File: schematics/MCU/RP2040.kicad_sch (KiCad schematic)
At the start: 38 parts, among them J2 Conn_ARM_SWD_TagConnect_TC203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, Q1 2N7002VC-7, SW1 TL3780AF240QG, U3 XC6210B332MR, U4 GD25Q127CWIGR

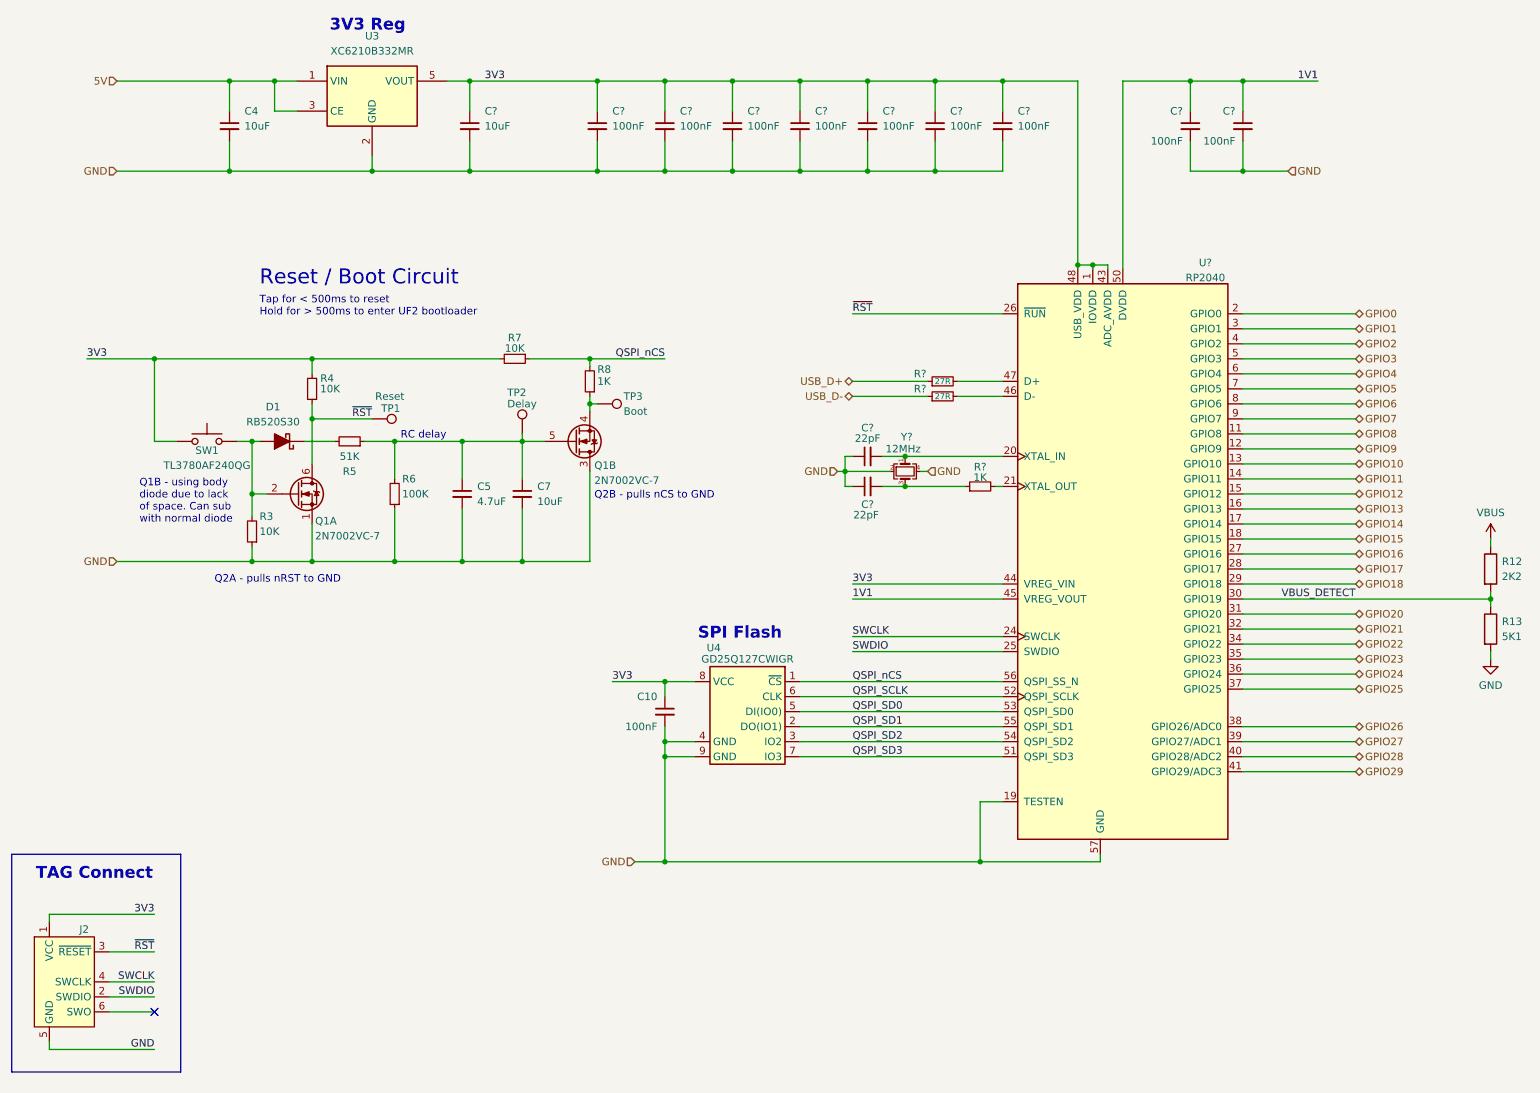
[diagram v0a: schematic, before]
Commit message: Minor refactor, add RP2040 controller schematic
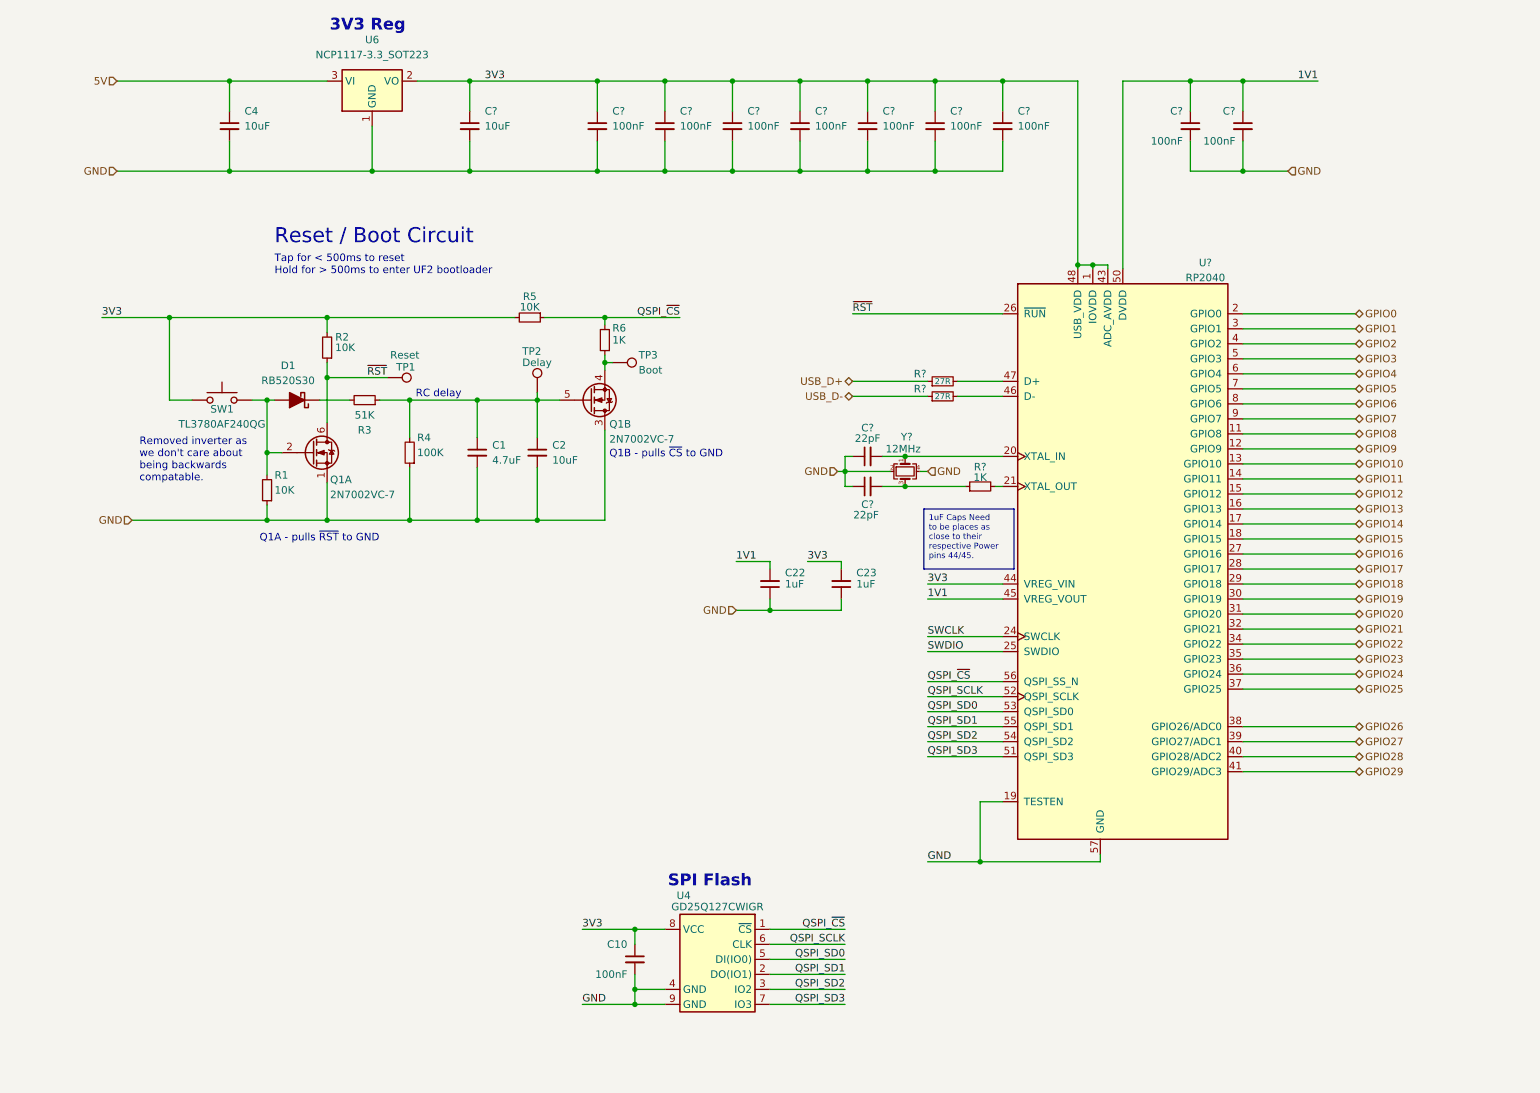
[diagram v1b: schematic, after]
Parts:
- removed C5: 4.7uF, Capacitor_SMD:C_0805_2012Metric, symbol Device:C_Small
- removed C7: 10uF, Capacitor_SMD:C_0805_2012Metric, symbol Device:C_Small
- removed J2: Conn_ARM_SWD_TagConnect_TC2030-NL, Connector:Tag-Connect_TC2030-IDC-NL_2x03_P1.27mm_Vertical, symbol Connector:Conn_ARM_SWD_TagConnect_TC2030-NL
- removed R12: 2K2, Resistor_SMD:R_0402_1005Metric, symbol Device:R
- removed R13: 5K1, Resistor_SMD:R_0402_1005Metric, symbol Device:R
- removed R7: 10K, Resistor_SMD:R_0402_1005Metric, symbol Device:R_Small
- removed R8: 1K, Resistor_SMD:R_0402_1005Metric, symbol Device:R_Small
- removed U3: XC6210B332MR, Package_TO_SOT_SMD:SOT-23-5, symbol Regulator_Linear:XC6210B332MR
- added C1: 4.7uF, Capacitor_SMD:C_0805_2012Metric, symbol Device:C_Small
- added C2: 10uF, Capacitor_SMD:C_0805_2012Metric, symbol Device:C_Small
- added C22, C23: 1uF, Capacitor_SMD:C_0603_1608Metric, symbol Device:C_Small
- added R1, R2: 10K, Resistor_SMD:R_0402_1005Metric, symbol Device:R_Small
- added U6: NCP1117-3.3_SOT223, Package_TO_SOT_SMD:SOT-223-3_TabPin2, symbol Regulator_Linear:NCP1117-3.3_SOT223
- C4, C?: footprint Capacitor_SMD:C_0402_1005Metric -> Capacitor_SMD:C_0805_2012Metric
- R3: value 10K -> 51K; MPN RC0402FR-0710KL -> RC0402FR-0751KL; Rating RES 10K OHM 1% 1/16W 0402 -> RES 51K OHM 1% 1/16W 0402; Supplier PN 311-10.0KLRCT-ND -> 311-51.0KLRCT-ND
- R4: value 10K -> 100K; MPN RC0402FR-0710KL -> RC0402FR-07100KL; Rating RES 10K OHM 1% 1/16W 0402 -> RES 100K OHM 1% 1/16W 0402; Supplier PN 311-10.0KLRCT-ND -> 311-100KLRCT-ND
- R5: value 51K -> 10K; MPN RC0402FR-0751KL -> RC0402FR-0710KL; Rating RES 51K OHM 1% 1/16W 0402 -> RES 10K OHM 1% 1/16W 0402; Supplier PN 311-51.0KLRCT-ND -> 311-10.0KLRCT-ND
- R6: value 100K -> 1K; MPN RC0402FR-07100KL -> RC0402FR-071KL; Rating RES 100K OHM 1% 1/16W 0402 -> RES 1K OHM 1% 1/16W 0402; Supplier PN 311-100KLRCT-ND -> 311-1.00KLRCT-ND
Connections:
- net 1V1: now also C22.2
- net 3V3: now also R5.2, C23.2, R2.2, U6.2 (VO); no longer R4.2
- net 5V: now also U6.3 (VI)
- net GND: now also R4.1, C1.2, C2.2, C22.1, C23.1, R1.1, U6.1 (GND); no longer R3.1, R6.1
- net ~{RST}: now also R2.1; no longer R4.1
- net at Q1.4 (S), TP3.1: now also R6.1
- net at Q1.5 (G), TP2.1: now also R3.1, R4.2, C1.1, C2.1; no longer R5.1, R6.2
- net at D1.2 (A), Q1.2 (G), SW1.1: now also R1.2; no longer R3.2
- net at D1.1 (K): now also R3.2; no longer R5.2
- net QSPI_nCS renamed QSPI_~{CS}
- net QSPI_~{CS}: now also R5.1, R6.2
- net VBUS_DETECT renamed GPIO19
- no-connect marks 1 -> 0
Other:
- note added: "Q1A - pulls ~{RST} to GND"
- note added: "Q1B - pulls ~{CS} to GND"
- note added: "Removed inverter as we don't care about being backwards compatable."
- note removed: "Q1B - using body diode due to lack of space. Can sub with normal diode"
- note removed: "Q2A - pulls nRST to GND"
- note removed: "Q2B - pulls nCS to GND"
- note removed: "TAG Connect"
- moved on the sheet: C10, U4

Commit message: Refactor RP2040, change to oscillator over crystal
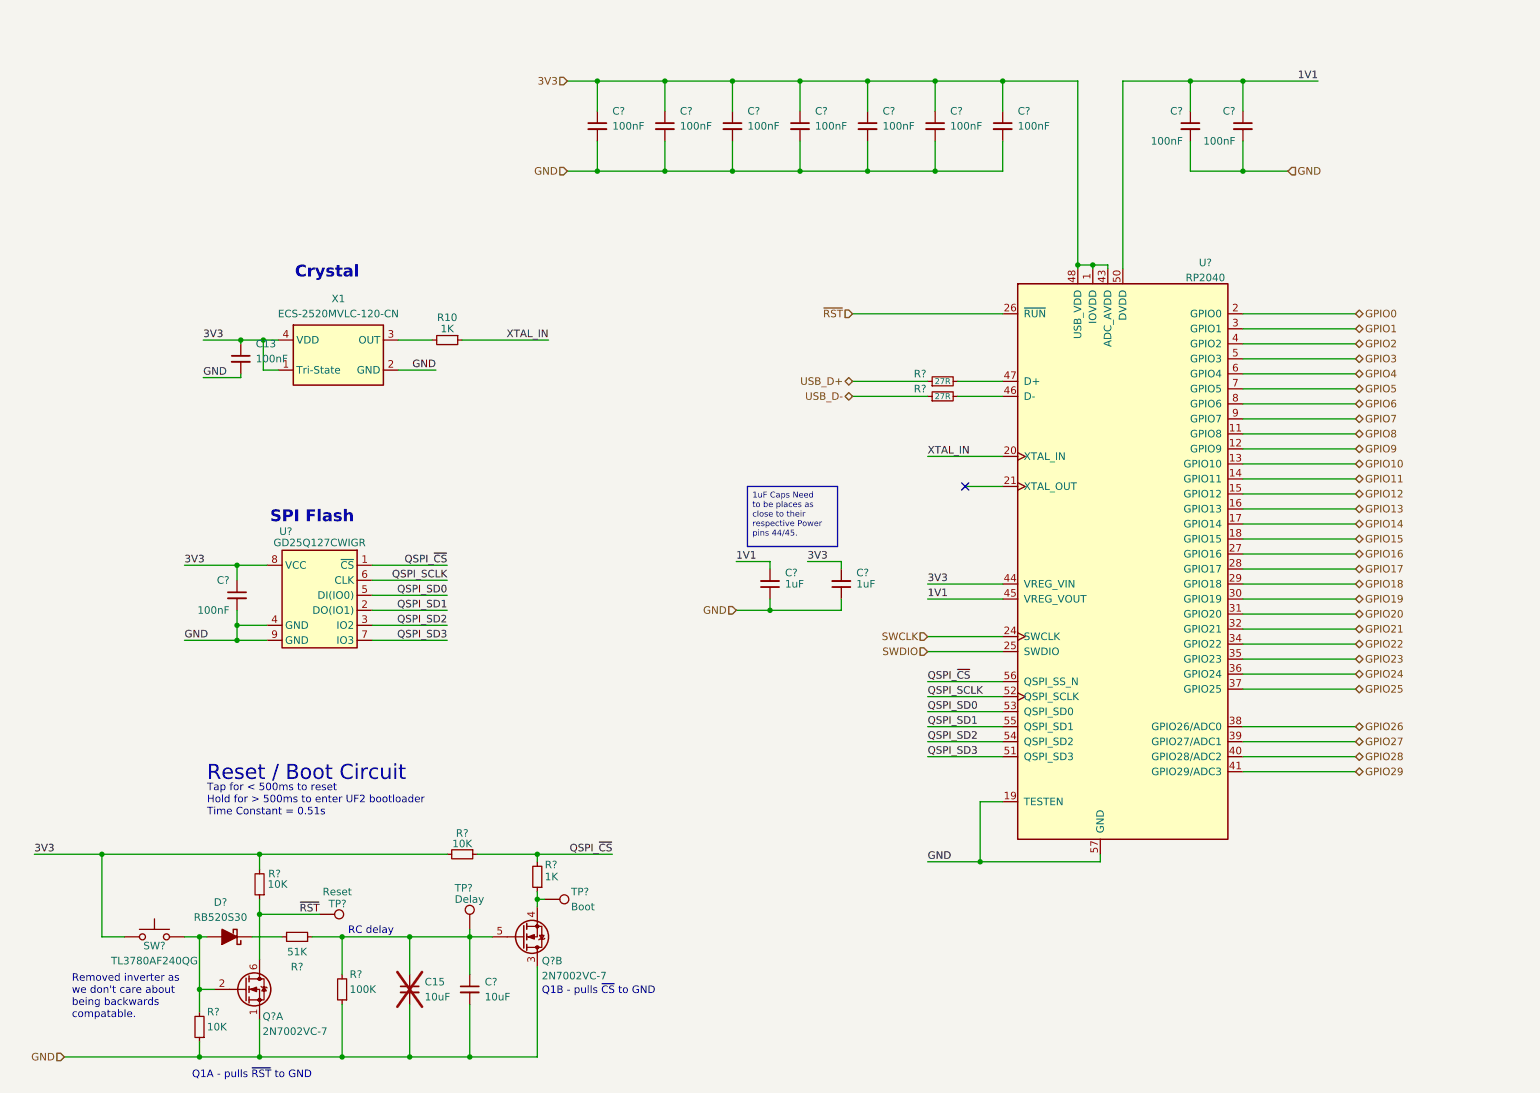
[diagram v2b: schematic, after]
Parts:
- removed C1: 4.7uF, Capacitor_SMD:C_0805_2012Metric, symbol Device:C_Small
- removed C4, C?: 10uF, Capacitor_SMD:C_0805_2012Metric, symbol Device:C_Small
- removed C? (x2): 22pF, Capacitor_SMD:C_0402_1005Metric, symbol Device:C_Small
- removed R?: 1K, Resistor_SMD:R_0402_1005Metric, symbol Device:R_Small
- removed U6: NCP1117-3.3_SOT223, Package_TO_SOT_SMD:SOT-223-3_TabPin2, symbol Regulator_Linear:NCP1117-3.3_SOT223
- removed Y?: 12MHz, Crystal:Crystal_SMD_Abracon_ABM8G-4Pin_3.2x2.5mm, symbol Device:Crystal_GND24_Small
- added C13: 100nF, Capacitor_SMD:C_0402_1005Metric, symbol Device:C_Small
- added C15: 10uF, Capacitor_SMD:C_0805_2012Metric, symbol Device:C_Small
- added R10: 1K, Resistor_SMD:R_0402_1005Metric, symbol Device:R_Small
- added X1: ECS-2520MVLC-120-CN, Mad_Footprints:Crystal_SMD_ECX-32-4Pin_3.2x2.5mm, symbol Mad_Symbols:ECS-2520MV-xxx-xx
- C? (x9): MPN C0402C104K3RAC7867 -> CC0402KPX7R9BB104; Manufacturer KEMET -> YAGEO; Price $0.33 -> $0.17; Rating CAP CER 0.1UF 25V X7R 0402 -> CAP 0402 50V 100 NF X7R; Supplier PN 399-14148-1-ND -> 13-CC0402KPX7R9BB104CT-ND
- C?: renamed from C2; MPN C0805C106K3PAC7800 -> CC0805KKX5R8BB106; Manufacturer KEMET -> YAGEO; Price $0.43 -> $0.47; Supplier PN 399-11939-1-ND -> 311-1869-1-ND
- C?: renamed from C10; MPN C0402C104K3RAC7867 -> CC0402KPX7R9BB104; Manufacturer KEMET -> YAGEO; Price $0.33 -> $0.17; Rating CAP CER 0.1UF 25V X7R 0402 -> CAP 0402 50V 100 NF X7R; Supplier PN 399-14148-1-ND -> 13-CC0402KPX7R9BB104CT-ND
- R? (x2): Rating RES 27 Ohms ±1% 0.063W, 1/16W Chip Resistor 0402 (1005 Metr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 -> RES 27 OHM 1% 1/16W 0402
- renumbered C22 to C?, C23 to C?, D1 to D?, Q1 to Q?, R2 to R?, R1 to R?, R4 to R?, R6 to R?, R3 to R?, R5 to R?, SW1 to SW?, TP2 to TP?, TP3 to TP?, TP1 to TP?, U4 to U?
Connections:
- net 3V3: now also C13.1, X1.1 (Tri-State), X1.4 (VDD)
- net GND: now also C13.2, C15.2, X1.2 (GND)
- net at C?.1, Q?.5 (G), R?.1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: now also C15.1
- net XTAL_IN: now reaches U?.20 (XTAL_IN)
- net XTAL_IN: now also R10.1
- new net: R10.2, X1.3 (OUT)
- no-connect marks 0 -> 1
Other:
- note added: "Crystal"
- note added: "Tap for < 500ms to reset Hold for > 500ms to enter UF2 bootloader Time Constant = 0.51s"
- note removed: "3V3 Reg"
- note removed: "Tap for < 500ms to reset Hold for > 500ms to enter UF2 bootloader"
- moved on the sheet: C?, D?, Q?A, Q?B, R?, SW?, TP?, U?

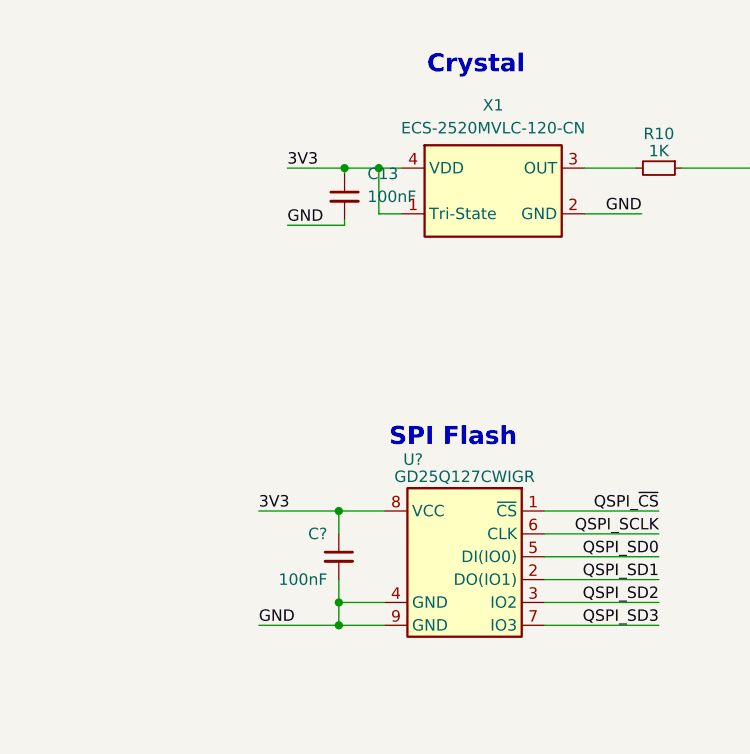
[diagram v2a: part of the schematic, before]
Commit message: Cleanup, BOM Update, Expose LED DOUT for internal status led
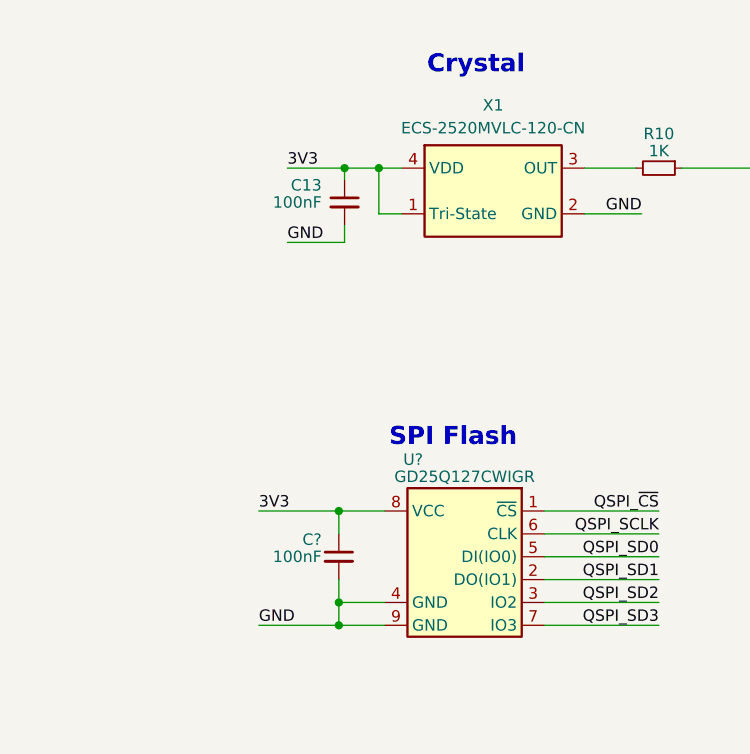
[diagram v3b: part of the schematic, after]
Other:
- moved on the sheet: C13
